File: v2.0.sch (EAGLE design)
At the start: 283 parts, among them J1 DC-044-A, J10 16p-2.54, J11 16p-2.54, J2 MICROSD-9P, J3 2p-2.54, J4 2p-2.54, J5 16p-2.54, J6 16p-2.54, J7 16p-2.54, J8 2p-2.54, J9 16p-2.54, Q1 32.768khZ@6Pf, Q2 SSM3J328R,LF, Q3 BSS138W-7-F, Q4 BSS138W-7-F, Q5 SSM3J328R,LF, Q6 BSS138W-7-F, Q7 BSS138W-7-F, Q8 CJ2305, SW1 MK-12C02 G1.5, SW3 MK-12C02 G1.5, SW4 MK-12C02 G1.5, SW5 TS-1101F, U1 MCP23017-E/SO, U10 74HCT139D, U11 BZX84C30, U12 SP483ECN-L, U13 FT232RL-SSOP28, U14 FT232RL-SSOP28, U15 FT232RL-SSOP28, U2 MCP79412-I/SN, U3 LOPY, U4 MAX213IDBR, U5 FT232RL-SSOP28, U6 FT232RL-SSOP28, U8 BR24G32-3, Y2 12MHZ

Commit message: Start of mods for V2
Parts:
- removed SW5: TS-1101F, Seeed-Switch-2016:DIP-BUTTON(2P-6.0X3.0X4.3MM)-TS-1101F
- added SW2: MK-12C02 G1.5, Seeed-Switch:SMD-TOGGLE-SWITCH-ON-ON(3+4P-6.7X2.7MM)
- F1: device Seeed-OPL-2017-01-Fuse-Akita:307010005_DIP_PPTC_4A_0310 -> imported-parts:307010005_DIP_PPTC_4A_0310
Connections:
- net +5V: now also Q2.S; no longer Q2.D
- net 5V_USB_HUB_FERRITE: now also SW2.A; no longer SW5.2
- net FTDI_HUB_LEDS: now also SW2.COM; no longer SW5.1
- net GND: now also SW2.SS1, SW2.SS2, SW2.SS3, SW2.SS4
- net N$122: now also Q2.D; no longer Q2.S
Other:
- moved on the sheet: D20, D21, Q2, R33, R34

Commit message: More work on fixing bugs
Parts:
- added Q10, Q9: S8550, Seeed-Transistor:SMD-TRANSISTORS-PNP-25V-500MA-S8550(SOT-23)
- added R26: 10K, Seeed-Resistor:SMD-RES-10K-1%-1/10W(0603)
- added R47: 47K, Seeed-Resistor:SMD-RES-47K-5%-1/10W(0603)
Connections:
- new net N$14: Q10.B, Q10.C, Q9.B, R26.2
- new net N$15: Q5.G, Q9.C, R47.2
- net GND: now also R26.1, R47.1; no longer Q5.G
- net LOPY_3V3: now also Q8.S; no longer Q8.D
- net LOPY_MISO: now also Q8.D; no longer Q8.S
- net N$122: now also Q10.E
- net PI_5V: now also Q9.E
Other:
- moved on the sheet: Q8
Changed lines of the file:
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@@
 <part name="SW2" library="Seeed-Switch" deviceset="SMD-TOGGLE-SWITCH-ON-ON(3+4P-6.7X2.7MM)" device="" value="MK-12C02 G1.5"/>
 <part name="GND96" library="supply1" library_urn="urn:adsk.eagle:library:371" deviceset="GND" device=""/>
+<part name="Q9" library="Seeed-Transistor" deviceset="SMD-TRANSISTORS-PNP-25V-500MA-S8550(SOT-23)" device="" value="S8550"/>
+<part name="Q10" library="Seeed-Transistor" deviceset="SMD-TRANSISTORS-PNP-25V-500MA-S8550(SOT-23)" device="" value="S8550"/>
+<part name="R26" library="Seeed-Resistor" deviceset="SMD-RES-10K-1%-1/10W(0603)" device="" value="10K"/>
+<part name="R47" library="Seeed-Resistor" deviceset="SMD-RES-47K-5%-1/10W(0603)" device="" value="47K"/>
 </parts>
 <sheets>
@@
 <instance part="GND76" gate="1" x="48.26" y="-21.59"/>
 <instance part="R46" gate="G$1" x="52.07" y="3.81" rot="R90"/>
-<instance part="Q8" gate="G$1" x="64.77" y="0"/>
+<instance part="Q8" gate="G$1" x="66.04" y="0" rot="MR180"/>
 </instances>
 <busses>
@@
 <pinref part="J4" gate="G$1" pin="1"/>
 <label x="76.2" y="7.62" size="1.778" layer="95"/>
-<pinref part="Q8" gate="G$1" pin="D"/>
-<wire x1="86.36" y1="7.62" x2="64.77" y2="7.62" width="0.1524" layer="91"/>
-<wire x1="64.77" y1="7.62" x2="64.77" y2="5.08" width="0.1524" layer="91"/>
+<wire x1="86.36" y1="7.62" x2="66.04" y2="7.62" width="0.1524" layer="91"/>
 <pinref part="R46" gate="G$1" pin="2"/>
-<wire x1="52.07" y1="7.62" x2="64.77" y2="7.62" width="0.1524" layer="91"/>
-<junction x="64.77" y="7.62"/>
+<pinref part="Q8" gate="G$1" pin="S"/>
+<wire x1="66.04" y1="7.62" x2="52.07" y2="7.62" width="0.1524" layer="91"/>
+<wire x1="66.04" y1="5.08" x2="66.04" y2="7.62" width="0.1524" layer="91"/>
+<junction x="66.04" y="7.62"/>
 </segment>
 <segment>
@@
 <label x="76.2" y="2.54" size="1.778" layer="95"/>
 <wire x1="77.47" y1="2.54" x2="77.47" y2="-5.08" width="0.1524" layer="91"/>
-<pinref part="Q8" gate="G$1" pin="S"/>
-<wire x1="77.47" y1="-5.08" x2="64.77" y2="-5.08" width="0.1524" layer="91"/>
+<pinref part="Q8" gate="G$1" pin="D"/>
+<wire x1="77.47" y1="-5.08" x2="66.04" y2="-5.08" width="0.1524" layer="91"/>
 </segment>
 </net>
@@
 <net name="N$13" class="0">
 <segment>
-<pinref part="Q8" gate="G$1" pin="G"/>
 <pinref part="R46" gate="G$1" pin="1"/>
-<wire x1="59.69" y1="0" x2="52.07" y2="0" width="0.1524" layer="91"/>
 <pinref part="Q7" gate="G$1" pin="D"/>
 <wire x1="52.07" y1="-2.54" x2="52.07" y2="0" width="0.1524" layer="91"/>
+<pinref part="Q8" gate="G$1" pin="G"/>
+<wire x1="60.96" y1="0" x2="52.07" y2="0" width="0.1524" layer="91"/>
 <junction x="52.07" y="0"/>
 </segment>
@@
 <instance part="SW3" gate="G$1" x="189.23" y="228.6" rot="MR180"/>
 <instance part="GND95" gate="1" x="182.88" y="208.28"/>
+<instance part="Q9" gate="G$1" x="248.92" y="212.09"/>
+<instance part="Q10" gate="G$1" x="234.95" y="212.09" rot="MR0"/>
+<instance part="R26" gate="G$1" x="232.41" y="203.2" rot="R90"/>
+<instance part="R47" gate="G$1" x="251.46" y="203.2" rot="R90"/>
 </instances>
 <busses>
@@
 <segment>
 <wire x1="195.58" y1="198.12" x2="203.2" y2="198.12" width="0.1524" layer="91"/>
-<pinref part="Q5" gate="G$1" pin="G"/>
 <wire x1="203.2" y1="198.12" x2="214.63" y2="198.12" width="0.1524" layer="91"/>
-<wire x1="214.63" y1="198.12" x2="241.3" y2="198.12" width="0.1524" layer="91"/>
-<wire x1="241.3" y1="198.12" x2="254" y2="198.12" width="0.1524" layer="91"/>
-<wire x1="241.3" y1="219.71" x2="241.3" y2="198.12" width="0.1524" layer="91"/>
-<junction x="241.3" y="198.12"/>
+<wire x1="214.63" y1="198.12" x2="232.41" y2="198.12" width="0.1524" layer="91"/>
 <pinref part="GND45" gate="1" pin="GND"/>
+<wire x1="232.41" y1="198.12" x2="251.46" y2="198.12" width="0.1524" layer="91"/>
+<wire x1="251.46" y1="198.12" x2="254" y2="198.12" width="0.1524" layer="91"/>
 <wire x1="195.58" y1="198.12" x2="195.58" y2="195.58" width="0.1524" layer="91"/>
 <pinref part="Q4" gate="G$1" pin="S"/>
@@
 <wire x1="203.2" y1="201.93" x2="203.2" y2="198.12" width="0.1524" layer="91"/>
 <junction x="203.2" y="198.12"/>
+<pinref part="R26" gate="G$1" pin="1"/>
+<wire x1="232.41" y1="199.39" x2="232.41" y2="198.12" width="0.1524" layer="91"/>
+<junction x="232.41" y="198.12"/>
+<pinref part="R47" gate="G$1" pin="1"/>
+<wire x1="251.46" y1="199.39" x2="251.46" y2="198.12" width="0.1524" layer="91"/>
+<junction x="251.46" y="198.12"/>
 </segment>
 <segment>
@@
 <label x="246.38" y="226.06" size="1.778" layer="95"/>
 <pinref part="TP11" gate="G$1" pin="TP"/>
-<wire x1="250.19" y1="224.79" x2="252.73" y2="224.79" width="0.1524" layer="91"/>
+<wire x1="250.19" y1="224.79" x2="251.46" y2="224.79" width="0.1524" layer="91"/>
 <junction x="250.19" y="224.79"/>
+<pinref part="Q9" gate="G$1" pin="E"/>
+<wire x1="251.46" y1="224.79" x2="252.73" y2="224.79" width="0.1524" layer="91"/>
+<wire x1="251.46" y1="217.17" x2="251.46" y2="224.79" width="0.1524" layer="91"/>
+<junction x="251.46" y="224.79"/>
 </segment>
 </net>
@@
 <wire x1="232.41" y1="224.79" x2="227.33" y2="224.79" width="0.1524" layer="91"/>
 <junction x="232.41" y="224.79"/>
-</segment>
-</net>
+<pinref part="Q10" gate="G$1" pin="E"/>
+<wire x1="232.41" y1="217.17" x2="232.41" y2="224.79" width="0.1524" layer="91"/>
+</segment>
+</net>
+<net name="N$14" class="0">
+<segment>
+<pinref part="Q10" gate="G$1" pin="C"/>
+<pinref part="R26" gate="G$1" pin="2"/>
+<wire x1="241.3" y1="212.09" x2="241.3" y2="207.01" width="0.1524" layer="91"/>
+<wire x1="232.41" y1="207.01" x2="237.49" y2="207.01" width="0.1524" layer="91"/>
+<junction x="232.41" y="207.01"/>
+<pinref part="Q10" gate="G$1" pin="B"/>
+<wire x1="237.49" y1="207.01" x2="241.3" y2="207.01" width="0.1524" layer="91"/>
+<wire x1="237.49" y1="212.09" x2="237.49" y2="207.01" width="0.1524" layer="91"/>
+<junction x="237.49" y="207.01"/>
+<pinref part="Q9" gate="G$1" pin="B"/>
+<wire x1="246.38" y1="212.09" x2="241.3" y2="212.09" width="0.1524" layer="91"/>
+</segment>
+</net>
+<net name="N$15" class="0">
+<segment>
+<pinref part="Q9" gate="G$1" pin="C"/>
+<pinref part="R47" gate="G$1" pin="2"/>
+<pinref part="Q5" gate="G$1" pin="G"/>
+<wire x1="241.3" y1="219.71" x2="243.84" y2="219.71" width="0.1524" layer="91"/>
+<wire x1="243.84" y1="219.71" x2="243.84" y2="207.01" width="0.1524" layer="91"/>
+<wire x1="243.84" y1="207.01" x2="251.46" y2="207.01" width="0.1524" layer="91"/>
+<junction x="251.46" y="207.01"/>
+</segment>
+</net>

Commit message: fixed name of pycom pin 12 signal track
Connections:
- net GPIO16 renamed GPIO6
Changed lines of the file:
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@@
 </segment>
 </net>
-<net name="GPIO16" class="0">
+<net name="GPIO6" class="0">
 <segment>
 <pinref part="PCB1" gate="G$1" pin="GPIO6"/>

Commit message: More updates to fix issues and start of v2 BOM
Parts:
- F1: value 307010005_DIP_PPTC_4A_0310 -> (none); device imported-parts:307010005_DIP_PPTC_4A_0310 -> imported-parts:FUSE-2920
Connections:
- removed net LOPY_P23: J7.6, J9.6, U3.P23
- new net LOPY_USD_SCLK: J2.SCLK, U3.P23
- net +5V: now also SW3.B
- net LOPY_3V3: no longer SW3.B
- net LOPY_3V3_FUSED: now also J7.6, J9.6; no longer J7.3, J9.3
- net LOPY_5V_FUSED: now also J7.3, J9.3
- net LOPY_CS1: now also J2.DO; no longer LOPY_SPI-3.S
- net LOPY_CS2: now also LOPY_SPI-3.S; no longer J2.CS
- net LOPY_MISO: no longer J2.DO
- net LOPY_MOSI: no longer J2.DI
- net LOPY_RXD1: now also J2.DI
- net LOPY_SCL/CLK: no longer J2.SCLK
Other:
- moved on the sheet: F59

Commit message: More updates, and verifing of current state of BOM
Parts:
- C31: device Seeed-Capacitor:CERAMIC-100NF-50V-10%-X7R(0805) -> Seeed-Capacitor:CERAMIC-100NF-50V-10%-X7R(0603)
- C40, C44, C48: value 47uf -> 4.7uf; device Seeed-Capacitor-2016:TANTALUM-SMD-47UF-6.3V(AVX-A) -> Seeed-Capacitor:TANTALUM-SMD-4.7UF-16V(AVX-A)
- F1: value (none) -> 1A
- R2: value 10K 1/10W -> 10K; device Seeed-Resistor:SMD-RES-10K-5%-1/10W(0603) -> Seeed-Resistor:SMD-RES-10K-1%-1/10W(0603)
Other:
- note added: "F1 = onecall 1822224"
- note removed: "my library"
- moved on the sheet: C12, C14, L2, L3, Q2, Q5, Q9, R47, TP11, TP12, TP2, TP3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

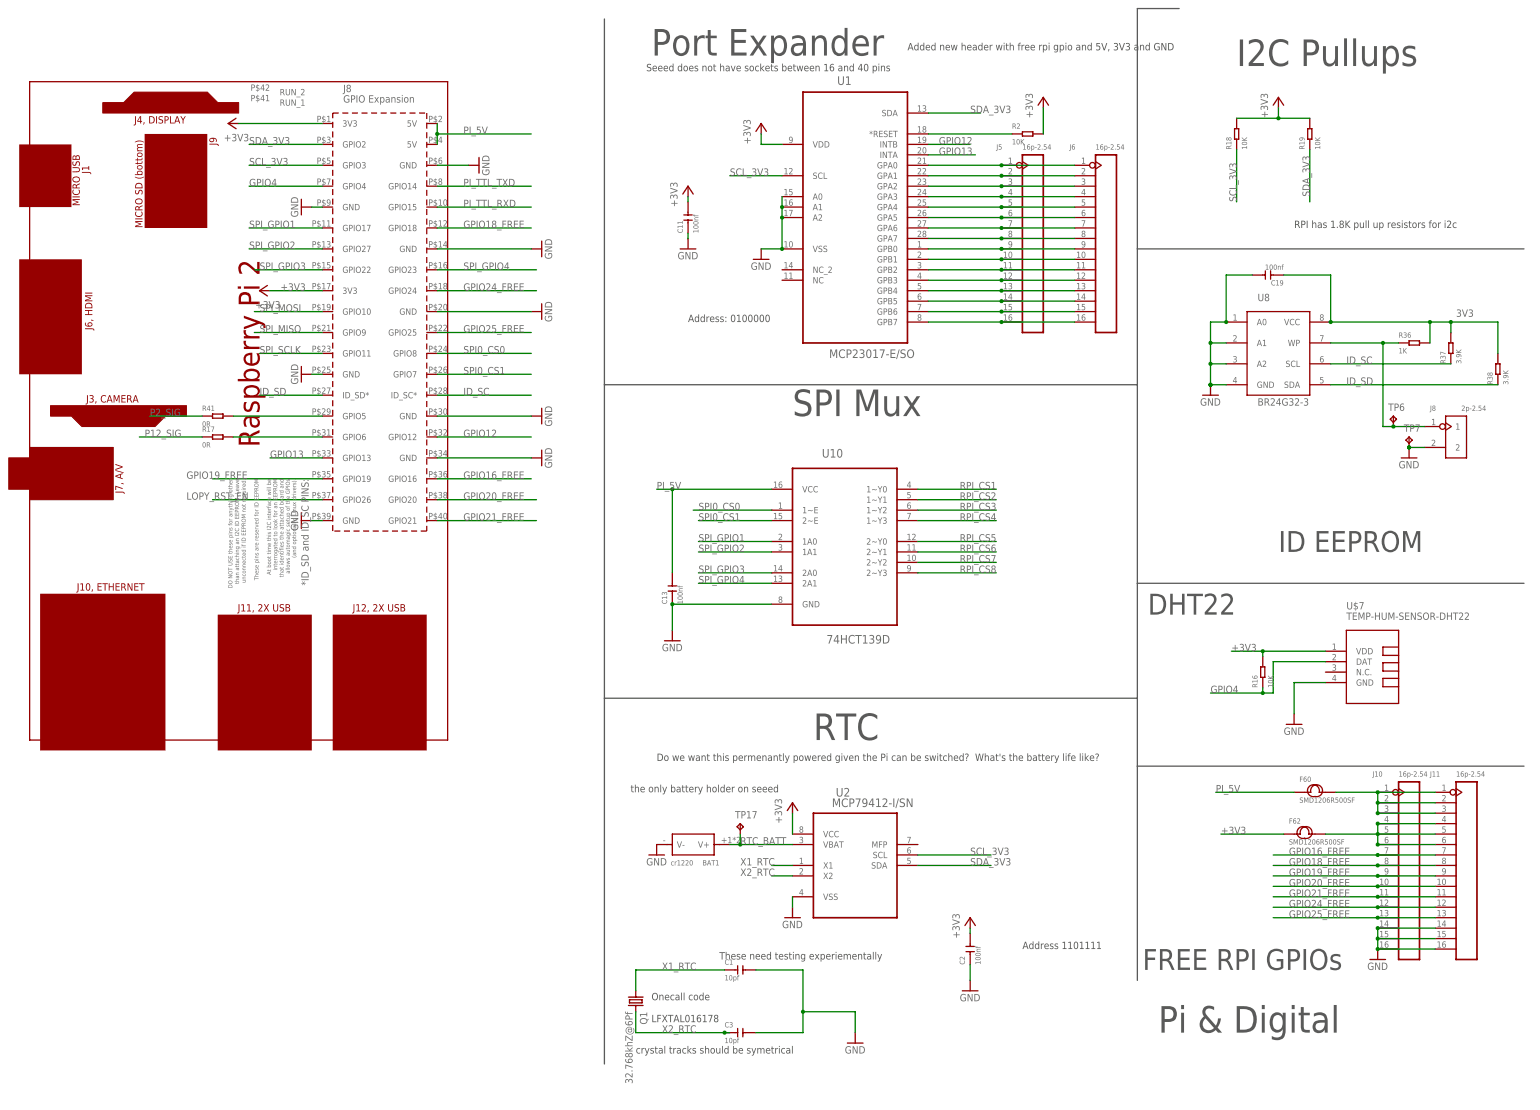
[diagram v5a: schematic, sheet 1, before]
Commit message: Lopy reset and bootloader now on port expander
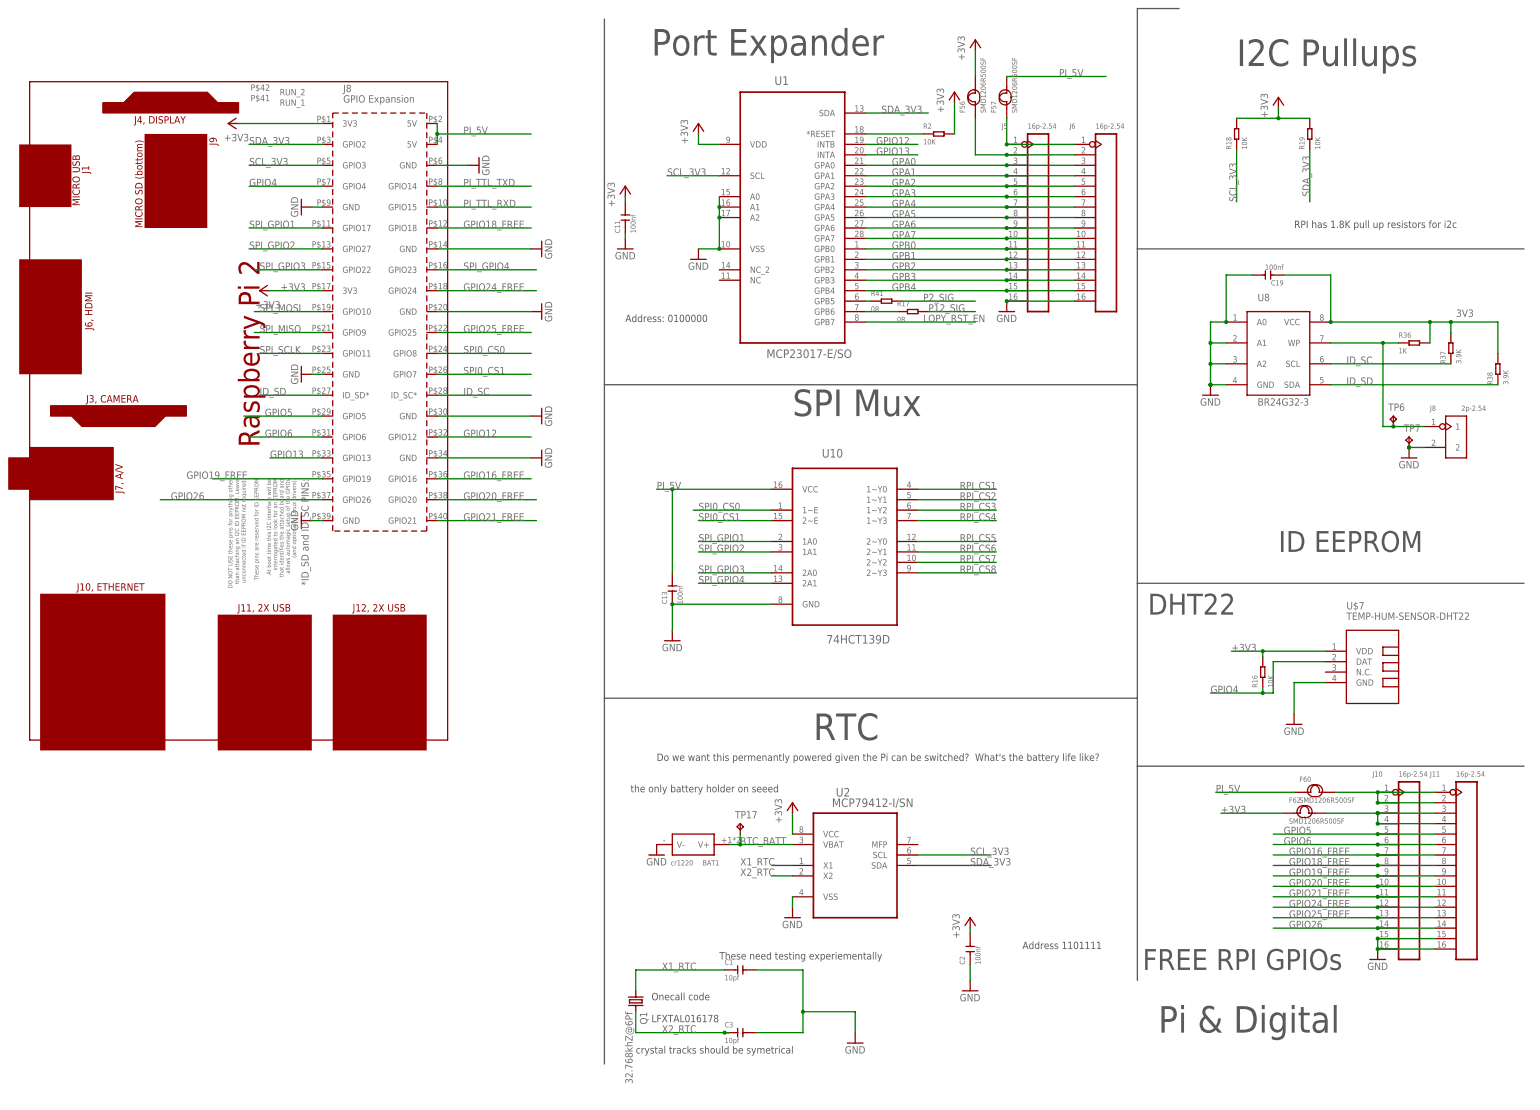
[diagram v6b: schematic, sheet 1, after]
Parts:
- added F56, F57: SMD1206R500SF, Seeed-Fuse:SMD-PPTC-500MA(1206)
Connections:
- removed net GPIO_3V3_FUSED: F62.2, J10.4, J10.5, J10.6, J11.4, J11.5, J11.6
- removed net GPIO_EXP_0: J5.1, J6.1, U1.GPA0
- removed net GPIO_EXP_1: J5.2, J6.2, U1.GPA1
- removed net GPIO_EXP_10: J5.11, J6.11, U1.GPB2
- removed net GPIO_EXP_11: J5.12, J6.12, U1.GPB3
- removed net GPIO_EXP_12: J5.13, J6.13, U1.GPB4
- removed net GPIO_EXP_13: J5.14, J6.14, U1.GPB5
- removed net GPIO_EXP_14: J5.15, J6.15, U1.GPB6
- removed net GPIO_EXP_15: J5.16, J6.16, U1.GPB7
- removed net GPIO_EXP_2: J5.3, J6.3, U1.GPA2
- removed net GPIO_EXP_3: J5.4, J6.4, U1.GPA3
- removed net GPIO_EXP_4: J5.5, J6.5, U1.GPA4
- removed net GPIO_EXP_5: J5.6, J6.6, U1.GPA5
- removed net GPIO_EXP_6: J5.7, J6.7, U1.GPA6
- removed net GPIO_EXP_7: J5.8, J6.8, U1.GPA7
- removed net GPIO_EXP_8: J5.9, J6.9, U1.GPB0
- removed net GPIO_EXP_9: J5.10, J6.10, U1.GPB1
- new net EXP_3V3: F56.1, J5.2, J6.2
- new net EXP_5V: F57.1, J5.1, J6.1
- new net GPA0: J5.3, J6.3, U1.GPA0
- new net GPA1: J5.4, J6.4, U1.GPA1
- new net GPA2: J5.5, J6.5, U1.GPA2
- new net GPA3: J5.6, J6.6, U1.GPA3
- new net GPA4: J5.7, J6.7, U1.GPA4
- new net GPA5: J5.8, J6.8, U1.GPA5
- new net GPA6: J5.9, J6.9, U1.GPA6
- new net GPA7: J5.10, J6.10, U1.GPA7
- new net GPB0: J5.11, J6.11, U1.GPB0
- new net GPB1: J5.12, J6.12, U1.GPB1
- new net GPB2: J5.13, J6.13, U1.GPB2
- new net GPB3: J5.14, J6.14, U1.GPB3
- new net GPB4: J5.15, J6.15, U1.GPB4
- new net GPIO26: J10.14, J11.14, PCB1.GPIO26
- new net N$16: R41.1, U1.GPB5
- new net N$18: R17.1, U1.GPB6
- new net N$19: F62.2, J10.3, J10.4, J11.3, J11.4
- net +3V3: now also F56.2
- net GND: now also J5.16, J6.16; no longer J10.14, J11.14
- net GPIO5: now also J10.5, J11.5; no longer R41.2
- net GPIO6: now also J10.6, J11.6; no longer R17.2
- net GPIO_5V_FUSED: no longer J10.3, J11.3
- net LOPY_RST_EN: now also U1.GPB7; no longer PCB1.GPIO26
- net P12_SIG: now also R17.2; no longer R17.1
- net P2_SIG: now also R41.2; no longer R41.1
- net PI_5V: now also F57.2
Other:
- note removed: "Added new header with free rpi gpio and 5V, 3V3 and GND"
- note removed: "Seeed does not have sockets between 16 and 40 pins"
- moved on the sheet: C11, F62, J5, J6, R17, R2, R41, U1
